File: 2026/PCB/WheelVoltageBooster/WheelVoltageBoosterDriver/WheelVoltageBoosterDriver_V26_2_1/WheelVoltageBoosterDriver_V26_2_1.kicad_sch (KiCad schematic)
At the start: 95 parts, among them J10 Conn_01x03_Socket, J11 Conn_01x05_Socket, J13 Conn_01x04_Socket, J2 Conn_01x02_Pin, J7 Conn_01x02_Pin, J8 Conn_01x07_Socket, J9 Conn_01x03_Socket, SW1 SW_MEC_5E, SW2 SW_MEC_5E, U1 MAX3051, U3 STM32H523CEU6, U4 TMP235AQDCKRQ1, U5 MAX20405AFOA/VY+, U6 MCP1703AT-3302E/CB, U7 MAX20405AFOA/VY+, Y1 Crystal_GND2

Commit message: 回路完成
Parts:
- removed C73, C74: 4.7u, Capacitor_SMD:C_0805_2012Metric_Pad1.18x1.45mm_HandSolder, symbol Device:C
- removed C75: 2.2u, Capacitor_SMD:C_0603_1608Metric_Pad1.08x0.95mm_HandSolder, symbol Device:C
- removed C76: 0.1u, Capacitor_SMD:C_0603_1608Metric_Pad1.08x0.95mm_HandSolder, symbol Device:C
- removed C77, C78, C79: 22u, Capacitor_SMD:C_0603_1608Metric_Pad1.08x0.95mm_HandSolder, symbol Device:C
- removed D7, D8: LED, WheelVoltageBooster_LIB_FTP:LED_1608_user_dif, symbol Device:LED
- removed L4: 1u, WheelVoltageBooster_LIB_FTP:74438366010, symbol Device:L
- removed R31, R32: 1k, Resistor_SMD:R_0603_1608Metric_Pad0.98x0.95mm_HandSolder, symbol Device:R
- removed R67: 10k, Resistor_SMD:R_0402_1005Metric_Pad0.72x0.64mm_HandSolder, symbol Device:R
- removed R68: 115k, Resistor_SMD:R_0402_1005Metric_Pad0.72x0.64mm_HandSolder, symbol Device:R
- removed U7: MAX20405AFOA/VY+, WheelVoltageBooster_LIB_FTP:MAX20405AFOFVY, symbol WheelVoltageBooster_LIB_SYM:MAX20405AFOA_VY+
- Y1: value Crystal_GND2 -> CSTNE16M0V530000R0
- gave numbers to parts that had none: 6
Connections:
- net +10V is gone; now on net 10V: R62.1
- net +20V is gone; now on net 25V: C64.1, C65.1, J11.2 (Pin_2), J13.2 (Pin_2), J2.1 (Pin_1), J7.1 (Pin_1), R15.1, R61.1, U5.3 (SUP), U5.9 (SUP)
- net +3V3 is gone; now on net 3V3: C1.1, C14.2, C15.2, C17.2, C18.2, C19.2, C2.1, C20.1, C22.1, C24.1, C72.1, J8.6 (Pin_6), R26.1, R35.1, R64.1, U1.3 (VDD), U2.4 (VDD), U3.1 (VBAT), U3.24 (VDD), U3.36 (VDD), U3.48 (VDD), U3.9 (VDDA), U4.4 (VDD), U6.2 (Vout)
- net Power_Circuit/10VEN: now reaches U3.14 (PA4)
- net +6V5 renamed 6V5
- no-connect marks 20 -> 16
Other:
- sheet Power_Circuit ports: added 10VEN; removed none
- moved on the sheet: C1, C12, C2, C24, C25, C26, C63, C64, C65, C66, C67, C68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

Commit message: FTP割り当て完了
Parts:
- J1, J3, J4, J5: footprint (none) -> Connector_PinSocket_2.54mm:PinSocket_1x04_P2.54mm_Vertical
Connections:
- net 3V3: now also J10.3 (Pin_3)
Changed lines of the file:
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@@
 	)
 	(junction
+		(at 128.27 45.72)
+		(diameter 0)
+		(color 0 0 0 0)
+	)
+	(junction
 		(at 245.11 43.18)
 		(diameter 0)
@@
 	(wire
 		(pts
+			(xy 128.27 45.72) (xy 128.27 48.26)
+		)
+		(stroke
+			(width 0)
+			(type default)
+		)
+	)
+	(wire
+		(pts
 			(xy 35.56 132.08) (xy 35.56 129.54)
 		)
@@
 			)
 		)
-		(property "Footprint" ""
+		(property "Footprint" "Connector_PinSocket_2.54mm:PinSocket_1x04_P2.54mm_Vertical"
 			(at 148.59 48.26 0)
 			(effects
@@
 			)
 		)
-		(property "Footprint" ""
+		(property "Footprint" "Connector_PinSocket_2.54mm:PinSocket_1x04_P2.54mm_Vertical"
 			(at 162.56 38.1 0)
 			(effects
@@
 			)
 		)
-		(property "Footprint" ""
+		(property "Footprint" "Connector_PinSocket_2.54mm:PinSocket_1x04_P2.54mm_Vertical"
 			(at 148.59 38.1 0)
 			(effects
@@
 			)
 		)
-		(property "Footprint" ""
+		(property "Footprint" "Connector_PinSocket_2.54mm:PinSocket_1x04_P2.54mm_Vertical"
 			(at 162.56 48.26 0)
 			(effects

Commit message: PCB60%完了
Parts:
- added J6: Conn_01x02_Pin, WheelVoltageBooster_LIB_FTP:AMASS_XT30PW-M_1x02_P2.50mm_Horizontal_ud, symbol Connector:Conn_01x02_Pin
- U3: footprint WheelVoltageBooster_LIB_FTP:ST32H523CEU6 -> UFQFPN-48_STM
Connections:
- net 25V: now also J6.2 (Pin_2)
- net GND: now also J6.1 (Pin_1)
- net USART1_RX: now also U3.28 (PB15/USART1_RX); no longer U3.27 (PB14/USART1_TX)
- net USART1_TX: now also U3.27 (PB14/USART1_TX); no longer U3.28 (PB15/USART1_RX)
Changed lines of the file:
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@@
 	(wire
 		(pts
+			(xy 132.08 63.5) (xy 134.62 63.5)
+		)
+		(stroke
+			(width 0)
+			(type default)
+		)
+	)
+	(wire
+		(pts
 			(xy 97.79 68.58) (xy 100.33 68.58)
 		)
@@
 	(wire
 		(pts
+			(xy 132.08 66.04) (xy 134.62 66.04)
+		)
+		(stroke
+			(width 0)
+			(type default)
+		)
+	)
+	(wire
+		(pts
 			(xy 77.47 25.4) (xy 77.47 35.56)
 		)
@@
 	)
 	(symbol
+		(lib_id "power:GND")
+		(at 134.62 63.5 90)
+		(unit 1)
+		(exclude_from_sim no)
+		(in_bom yes)
+		(on_board yes)
+		(dnp no)
+		(property "Reference" "#PWR0123"
+			(at 140.97 63.5 0)
+			(effects
+				(font
+					(size 1.27 1.27)
+				)
+				(hide yes)
+			)
+		)
+		(property "Value" "GND"
+			(at 138.43 63.5 0)
+			(effects
+				(font
+					(size 1.27 1.27)
+				)
+			)
+		)
+		(property "Footprint" ""
+			(at 134.62 63.5 0)
+			(effects
+				(font
+					(size 1.27 1.27)
+				)
+				(hide yes)
+			)
+		)
+		(property "Datasheet" ""
+			(at 134.62 63.5 0)
+			(effects
+				(font
+					(size 1.27 1.27)
+				)
+				(hide yes)
+			)
+		)
+		(property "Description" "Power symbol creates a global label with name \"GND\" , ground"
+			(at 134.62 63.5 0)
+			(effects
+				(font
+					(size 1.27 1.27)
+				)
+				(hide yes)
+			)
+		)
+		(pin "1"
+		)
+		(instances
+			(project "WheelVoltageBoosterDriver_V26_2_1"
+				(path "/80c9ed4f-d051-48b1-8382-19040773b73e"
+					(reference "#PWR0123")
+					(unit 1)
+				)
+			)
+		)
+	)
+	(symbol
 		(lib_id "Device:R")
 		(at 238.76 43.18 90)
@@
 	)
 	(symbol
+		(lib_id "power:+10V")
+		(at 134.62 66.04 270)
+		(unit 1)
+		(exclude_from_sim no)
+		(in_bom yes)
+		(on_board yes)
+		(dnp no)
+		(property "Reference" "#PWR035"
+			(at 130.81 66.04 0)
+			(effects
+				(font
+					(size 1.27 1.27)
+				)
+				(hide yes)
+			)
+		)
+		(property "Value" "25V"
+			(at 139.7 65.786 0)
+			(effects
+				(font
+					(size 1.27 1.27)
+				)
+			)
+		)
+		(property "Footprint" ""
+			(at 134.62 66.04 0)
+			(effects
+				(font
+					(size 1.27 1.27)
+				)
+				(hide yes)
+			)
+		)
+		(property "Datasheet" ""
+			(at 134.62 66.04 0)
+			(effects
+				(font
+					(size 1.27 1.27)
+				)
+				(hide yes)
+			)
+		)
+		(property "Description" "Power symbol creates a global label with name \"+10V\""
+			(at 134.62 66.04 0)
+			(effects
+				(font
+					(size 1.27 1.27)
+				)
+				(hide yes)
+			)
+		)
+		(pin "1"
+		)
+		(instances
+			(project "WheelVoltageBoosterDriver_V26_2_1"
+				(path "/80c9ed4f-d051-48b1-8382-19040773b73e"
+					(reference "#PWR035")
+					(unit 1)
+				)
+			)
+		)
+	)
+	(symbol
 		(lib_id "power:GND")
 		(at 245.11 60.96 0)
@@
 	)
 	(symbol
+		(lib_id "Connector:Conn_01x02_Pin")
+		(at 127 63.5 0)
+		(unit 1)
+		(exclude_from_sim no)
+		(in_bom yes)
+		(on_board yes)
+		(dnp no)
+		(fields_autoplaced yes)
+		(property "Reference" "J6"
+			(at 127.635 58.42 0)
+			(effects
+				(font
+					(size 1.27 1.27)
+				)
+			)
+		)
+		(property "Value" "Conn_01x02_Pin"
+			(at 127.635 60.96 0)
+			(effects
+				(font
+					(size 1.27 1.27)
+				)
+			)
+		)
+		(property "Footprint" "WheelVoltageBooster_LIB_FTP:AMASS_XT30PW-M_1x02_P2.50mm_Horizontal_ud"
+			(at 127 63.5 0)
+			(effects
+				(font
+					(size 1.27 1.27)
+				)
+				(hide yes)
+			)
+		)
+		(property "Datasheet" "~"
+			(at 127 63.5 0)
+			(effects
+				(font
+					(size 1.27 1.27)
+				)
+				(hide yes)
+			)
+		)
+		(property "Description" "Generic connector, single row, 01x02, script generated"
+			(at 127 63.5 0)
+			(effects
+				(font
+					(size 1.27 1.27)
+				)
+				(hide yes)
+			)
+		)
+		(pin "2"
+		)
+		(pin "1"
+		)
+		(instances
+			(project ""
+				(path "/80c9ed4f-d051-48b1-8382-19040773b73e"
+					(reference "J6")
+					(unit 1)
+				)
+			)
+		)
+	)
+	(symbol
 		(lib_id "Device:R")
 		(at 138.43 172.72 90)
@@
 			)
 		)
-		(property "Footprint" "WheelVoltageBooster_LIB_FTP:ST32H523CEU6"
+		(property "Footprint" "UFQFPN-48_STM"
 			(at 60.452 85.852 0)
 			(effects

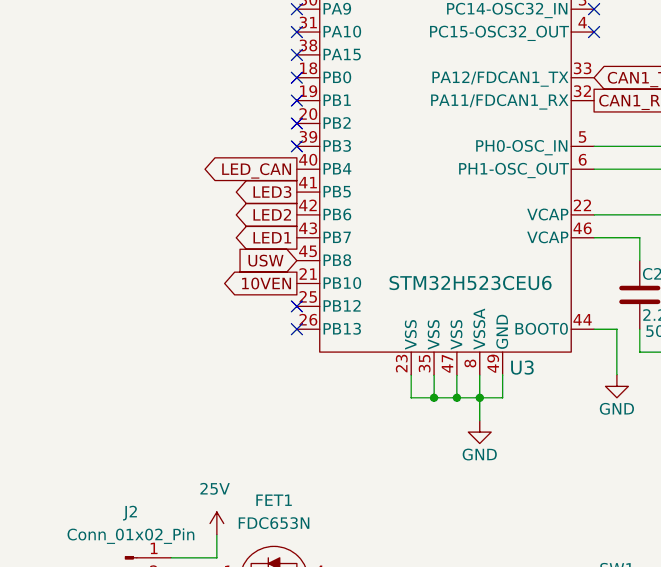
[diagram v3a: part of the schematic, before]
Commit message: 配線追加
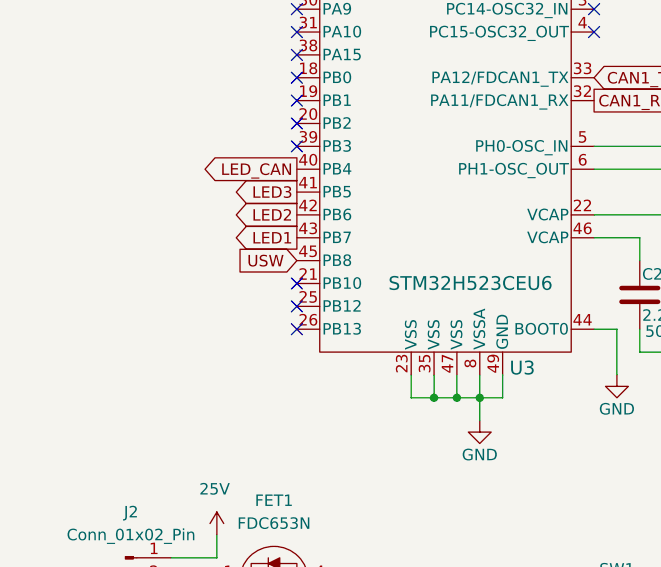
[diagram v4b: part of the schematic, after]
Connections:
- net 10VEN: no longer names the net of U3.21 (PB10)
- no-connect marks 16 -> 17
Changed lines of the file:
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@@
 	)
 	(no_connect
+		(at 44.45 101.6)
+	)
+	(no_connect
 		(at 77.47 68.58)
 	)
@@
 			(effects
 				(font
-					(size 1.27 1.27)
-				)
-				(justify right)
-				(hide yes)
-			)
-		)
-	)
-	(global_label "10VEN"
-		(shape output)
-		(at 44.45 101.6 180)
-		(fields_autoplaced yes)
-		(effects
-			(font
-				(size 1.27 1.27)
-			)
-			(justify right)
-		)
-		(property "Intersheetrefs" "${INTERSHEET_REFS}"
-			(at 35.4777 101.6 0)
-			(effects
-				(font

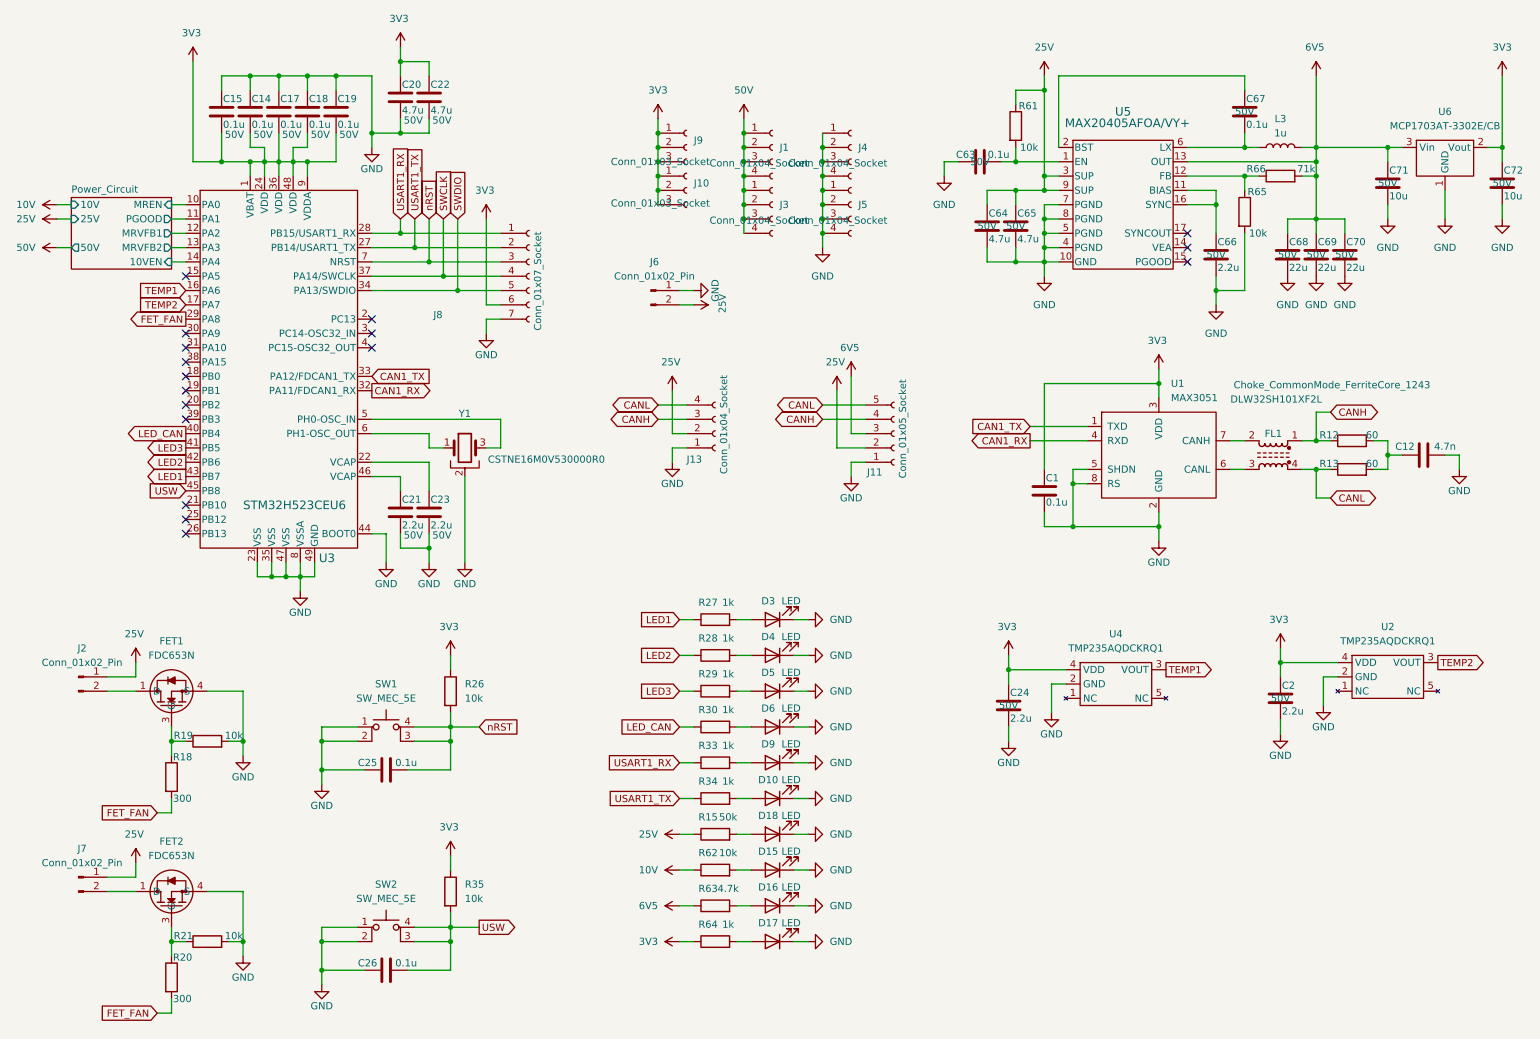
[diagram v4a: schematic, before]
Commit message: BIAS系統の配線完了
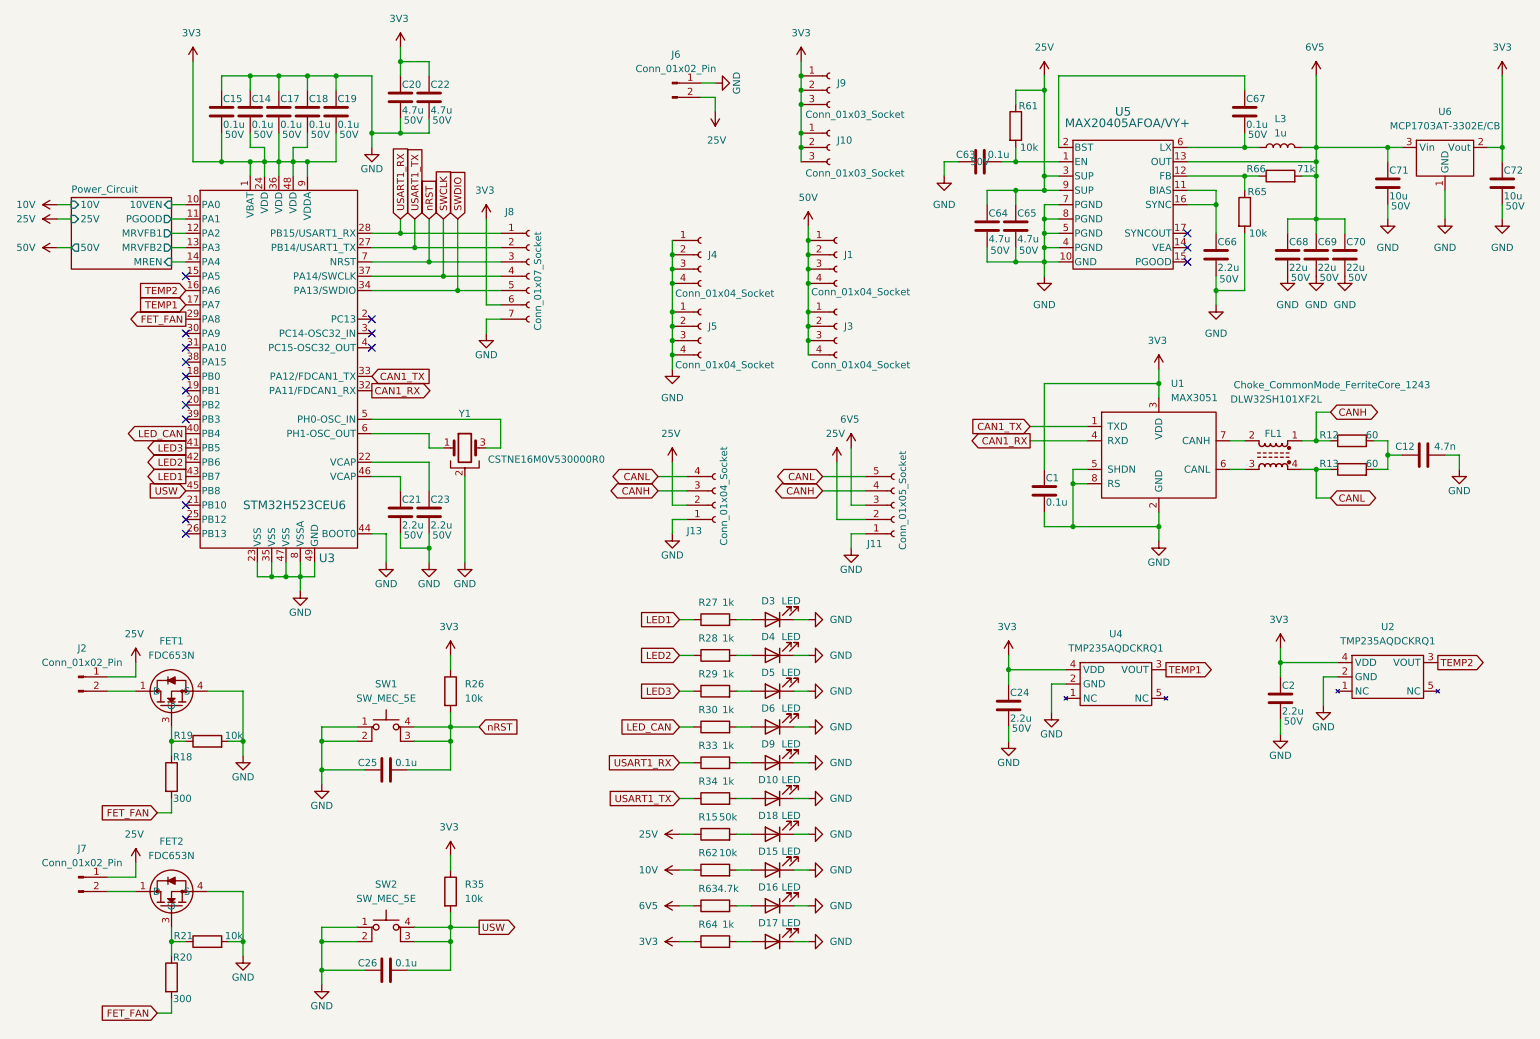
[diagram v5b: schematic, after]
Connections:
- net Power_Circuit/10VEN: now also U3.10 (PA0); no longer U3.14 (PA4)
- net Power_Circuit/MREN: now also U3.14 (PA4); no longer U3.10 (PA0)
- net TEMP1: now also U3.17 (PA7); no longer U3.16 (PA6)
- net TEMP2: now also U3.16 (PA6); no longer U3.17 (PA7)
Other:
- moved on the sheet: J1, J10, J11, J13, J3, J4, J5, J6, J9
